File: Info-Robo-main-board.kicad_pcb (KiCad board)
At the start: 4 copper layers, 50 x 100 mm, 110 parts, among them IC101 LM66100DCKT, IC102 LM66100DCKT, IC103 M78AR05-0.5, J101 XT60, J102 XH_4P, J103 XH_4P, J104 XH_4P, J105 XH_4P, J106 XH_4P, J107 XH_4P, J108 XH_4P, J109 XH_3P, J110 XH_3P, J111 XH_3P, J112 XH_3P, J113 XH_3P, J114 XH_3P, J115 XH_3P, J116 XH_3P, J117 XH_3P, J118 XH_3P, J119 XH_3P, J120 XH_3P, J121 XH_3P, J122 XH_3P, J123 XH_3P, J124 XH_3P, J201 TYPE-C-14PLC-H10.0, J202 Conn_01x01, J203 Conn_01x01, J204 Conn_01x01, J205 Conn_01x01, SW301 SW_Push_45deg, U101 AMS1117-3.3, U201 STM32F103CBTx, U301 STM32F446RETx, U401 MCP2562-E-P, U501 MCP2562-E-P, Y201 NX3225GD-8MHZ-STD-CRA-3, Y301 SX3B16.000F1510F30

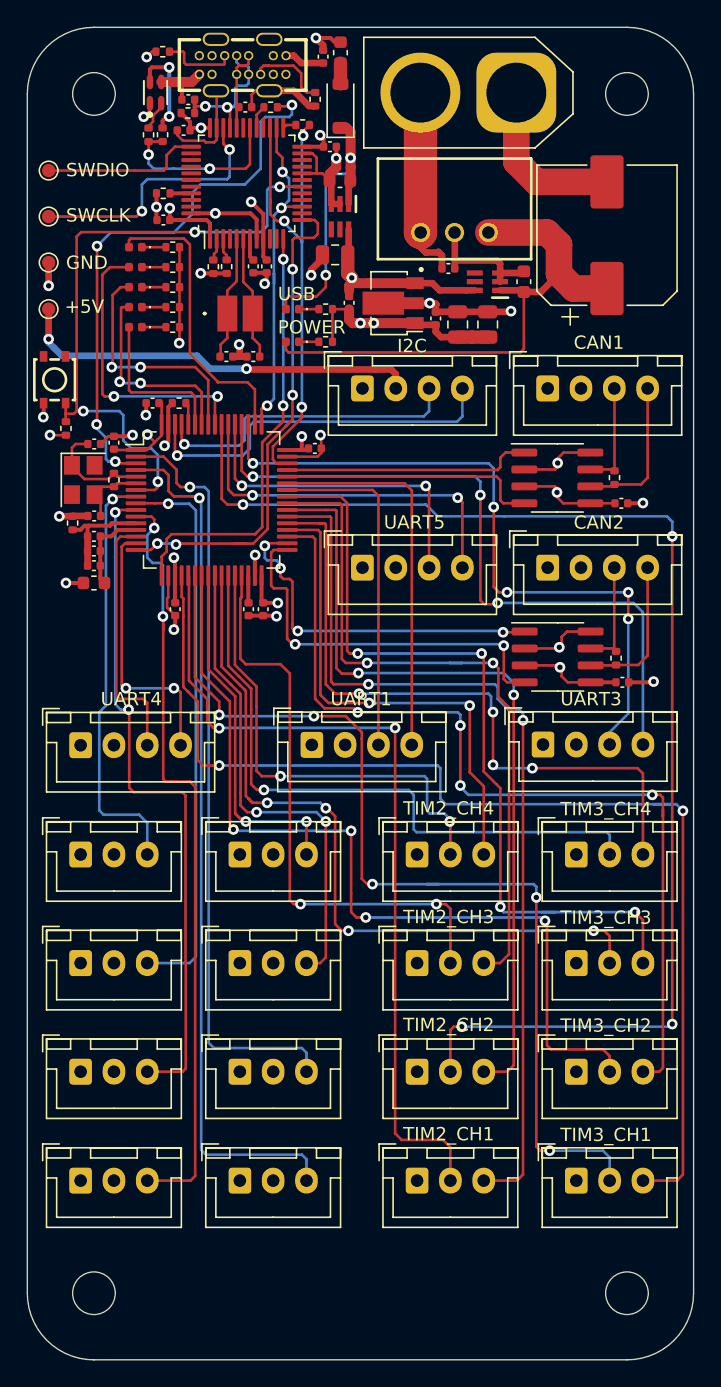
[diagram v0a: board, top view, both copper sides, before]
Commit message: Fix ST-link reset
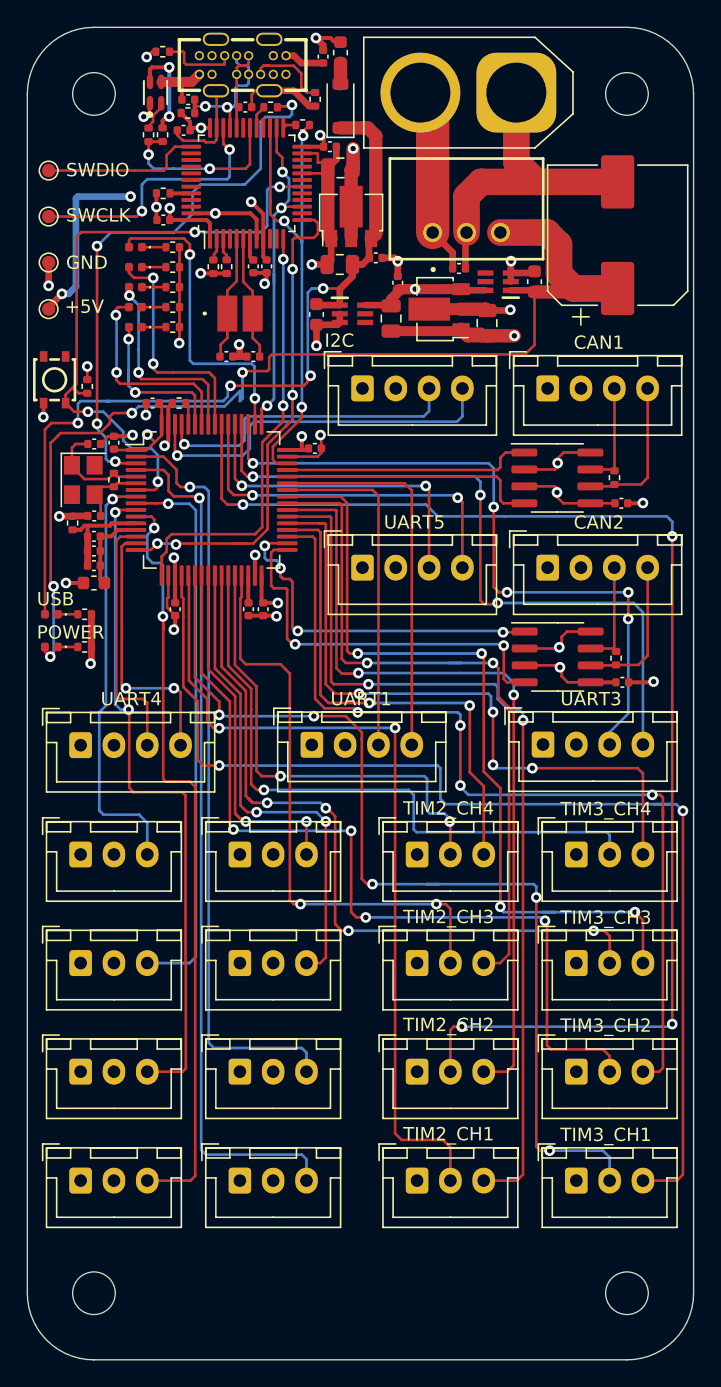
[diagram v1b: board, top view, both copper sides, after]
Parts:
- removed C204: 0.1uF, Capacitor_SMD:C_0402_1005Metric
- removed C205: 4.7uF, Capacitor_SMD:C_0805_2012Metric
- added C213: 10uF, Capacitor_SMD:C_0805_2012Metric, F.Cu at (123.5, 67.8)
- added C214: 0.1uF, Capacitor_SMD:C_0402_1005Metric, F.Cu at (126.2, 67.3)
- added C215: 10uF, Capacitor_SMD:C_0805_2012Metric, F.Cu at (123.5, 60.5)
- added U202: AMS1117-3.3, Package_TO_SOT_SMD:SOT-89-3, F.Cu at (124.3, 63.9)
- moved R107 29.2 mm to (104.3, 96.5)
- moved D107 29.2 mm to (101.8, 96.5)
- moved R106 29.2 mm to (104.3, 94.0)
- moved D106 29.2 mm to (101.8, 94.0)
- moved C101 10.2 mm to (121.7, 71.5), turned to -90 degrees
- moved IC101 7.35 mm to (124.4, 71.5), turned to 0 degrees
- moved C103 6.36 mm to (127.3, 71.8), turned to -90 degrees
- moved C104 3.95 mm to (127.8, 69.2), turned to 90 degrees
- moved R302 3.53 mm to (104.5, 77.0), turned to -90 degrees
- moved U101 3.48 mm to (130.6, 71.1)
- moved IC103 0.90 mm to (133.0, 67.4)
- moved C102 0.80 mm to (138.1, 69.1)
- moved C106 0.80 mm to (132.4, 68.1)
- moved IC102 0.80 mm to (135.3, 69.1)
- moved C107 0.80 mm to (144.3, 65.6)
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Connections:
- C209 pad 1: +3.3V -> /ST-LinkV2_1/ST-LIN3V3
- C210 pad 1: +3.3V -> /ST-LinkV2_1/ST-LIN3V3
- C211 pad 1: +3.3V -> /ST-LinkV2_1/ST-LIN3V3
- C212 pad 1: +3.3V -> /ST-LinkV2_1/ST-LIN3V3
- D202 pad 1: +3.3V -> /ST-LinkV2_1/ST-LIN3V3
- J205 pad 1: +5V -> /ST-LinkV2_1/ST-LIN3V3
- R208 pad 1: +3.3V -> /ST-LinkV2_1/ST-LIN3V3
- U201 pad 1: +3.3V -> /ST-LinkV2_1/ST-LIN3V3
- U201 pad 24: +3.3V -> /ST-LinkV2_1/ST-LIN3V3
- U201 pad 36: +3.3V -> /ST-LinkV2_1/ST-LIN3V3
- U201 pad 48: +3.3V -> /ST-LinkV2_1/ST-LIN3V3
- U201 pad 9: +3.3V -> /ST-LinkV2_1/ST-LIN3V3
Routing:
- net /ST-LinkV2_1/ST-LIN3V3: track 0.00 -> 70.2 mm, vias 0 -> 8
- net /VBUS_USB: track 22.2 -> 64.9 mm, vias 2 -> 4
- net /VIN: track 39.9 -> 79.4 mm, vias 0 -> 4
- net +5V: track 72.8 -> 36.0 mm, vias 5 -> 3
- net +3.3V: track 44.2 -> 23.3 mm, vias 13 -> 7
- net GND: track 131.6 -> 146.1 mm, vias 25 -> 27
- net /GPIO_out_PB4: track 22.1 -> 17.6 mm
- net /GPIO_out_PB5: track 17.8 -> 15.5 mm
- net /NRST: track 49.1 -> 47.2 mm
- net /GPIO_out_PA15: track 22.2 -> 23.4 mm, vias 0 -> 2
- net /GPIO_out_PB7: track 12.0 -> 12.9 mm, vias 0 -> 2
- net /GPIO_out_PB6: track 15.1 -> 15.6 mm
